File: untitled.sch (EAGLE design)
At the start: 6 parts, among them IC1 PIC16F877P

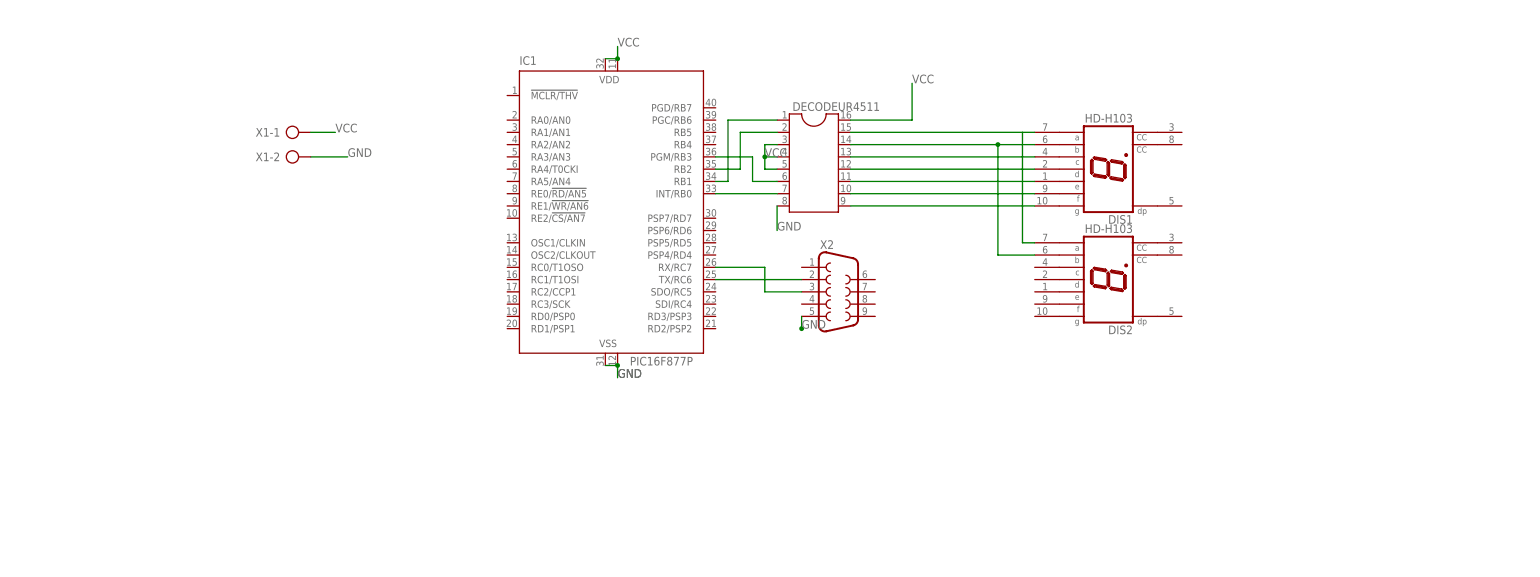
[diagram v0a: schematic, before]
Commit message: Fichier schéma eagle
Schéma eagle fini par Jarod Boulanger-Flémal.
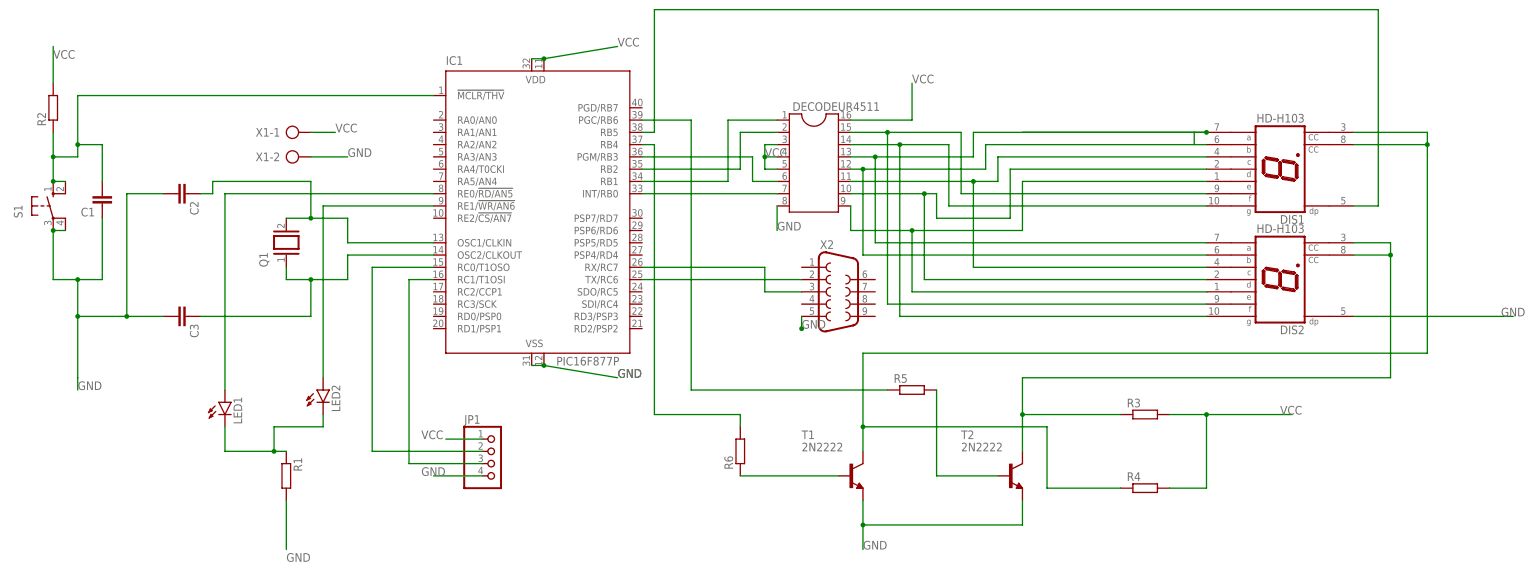
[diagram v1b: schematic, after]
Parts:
- added C1, C2, C3: (no value), rcl:C-EU025-025X050
- added JP1: (no value), pinhead:PINHD-1X4
- added LED1, LED2: (no value), led:LED5MM
- added Q1: (no value), special:XTAL/S
- added R1, R2, R3, R4, R5, R6: (no value), rcl:R-EU_0207/10
- added S1: (no value), switch-omron:10-XX
- added T1, T2: 2N2222, transistor-neu-to92:2N2222
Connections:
- new net N$14: IC1.RE0/!RD/AN5, LED1.A
- new net N$15: IC1.RB4, R6.2
- new net N$16: R6.1, T1.B
- new net N$17: DIS1.CC, DIS1.CC@1, R4.1, T1.C
- new net N$18: DIS1.DP, IC1.RB5
- new net N$19: IC1.PGC/RB6, R5.1
- new net N$20: R5.2, T2.B
- new net N$21: DIS2.CC, DIS2.CC@1, R3.1, T2.C
- new net N$23: IC1.RE1/!WR/AN6, LED2.A
- new net N$24: LED1.C, LED2.C, R1.1
- new net N$25: IC1.RC0/T1OSO, JP1.2
- new net N$26: C1.2, IC1.!MCLR/THV, R2.1, S1.S, S1.S1
- new net N$27: IC1.RC1/T1OSI, JP1.3
- new net N$30: C2.1, IC1.OSC1/CLKIN, Q1.2
- new net N$31: C3.1, IC1.OSC2/CLKOUT, Q1.1
- net GND: now also C1.1, C2.2, C3.2, DIS2.DP, JP1.4, R1.2, S1.P, S1.P1, T1.E, T2.E
- net N$10: now also DECODEUR4511.10, DIS2.D; no longer DECODEUR4511.12
- net N$11: now also DECODEUR4511.12, DIS1.B, DIS2.B; no longer DECODEUR4511.11, DIS1.E
- net N$12: now also DECODEUR4511.11, DIS1.C, DIS2.C; no longer DECODEUR4511.10, DIS1.F
- net N$13: now also DIS1.E, DIS2.E; no longer DIS1.G
- net N$7: now also DECODEUR4511.13; no longer DECODEUR4511.15
- net N$8: now also DECODEUR4511.15, DIS1.F, DIS2.F; no longer DECODEUR4511.14, DIS1.B, DIS2.B
- net N$9: now also DECODEUR4511.14, DIS1.G, DIS2.G; no longer DECODEUR4511.13, DIS1.C
- net VCC: now also JP1.1, R2.2, R3.2, R4.2
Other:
- moved on the sheet: DIS1, DIS2, IC1
